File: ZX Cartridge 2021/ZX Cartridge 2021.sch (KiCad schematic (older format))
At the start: 7 parts, among them J1 Cartridge, M1 Mounting, M2 Mounting, M3 Mounting, M4 Mounting, U1 27C512

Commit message: ... and the rest
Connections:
- net ~ROM_0: now also J1.A18 (~ROM_0); no longer J1.A20 (~ROM_2)
- net ~ROM_OE: now also J1.A17 (~ROM_OE); no longer J1.A21 (~ROM_3)
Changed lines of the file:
@@
 	1    0    0    -1
 $EndComp
-Text Label 8225 4400 1    50   ~ 0
+Text Label 8025 4400 1    50   ~ 0
 ~ROM_0
 Text Label 6625 2575 3    50   ~ 0
@@
 Wire Wire Line
 	6725 2550 6725 2900
-Text Label 8325 4400 1    50   ~ 0
+Text Label 7925 4400 1    50   ~ 0
 ~ROM_OE
 Wire Wire Line
@@
 	6925 2450 7025 2550
 Entry Wire Line
-	8325 4525 8225 4425
-Entry Wire Line
-	8425 4525 8325 4425
+	8125 4525 8025 4425
+Entry Wire Line
+	8025 4525 7925 4425
 Entry Wire Line
 	7525 4525 7425 4425
@@
 	8725 3975 8725 3900
 Wire Wire Line
-	8325 3900 8325 4425
-Wire Wire Line
-	8225 3900 8225 4425
+	7925 3900 7925 4425
+Wire Wire Line
+	8025 3900 8025 4425
 Wire Wire Line
 	7525 3900 7525 4425
@@
 NoConn ~ 6825 3900
 NoConn ~ 7625 3900
-NoConn ~ 7925 3900
-NoConn ~ 8025 3900
 NoConn ~ 8125 3900
 NoConn ~ 7025 3900
@@
 	3400 5375 5100 5375
 NoConn ~ 8425 3900
+NoConn ~ 8225 3900
+NoConn ~ 8325 3900
 Wire Bus Line
 	5100 2450 5100 5375

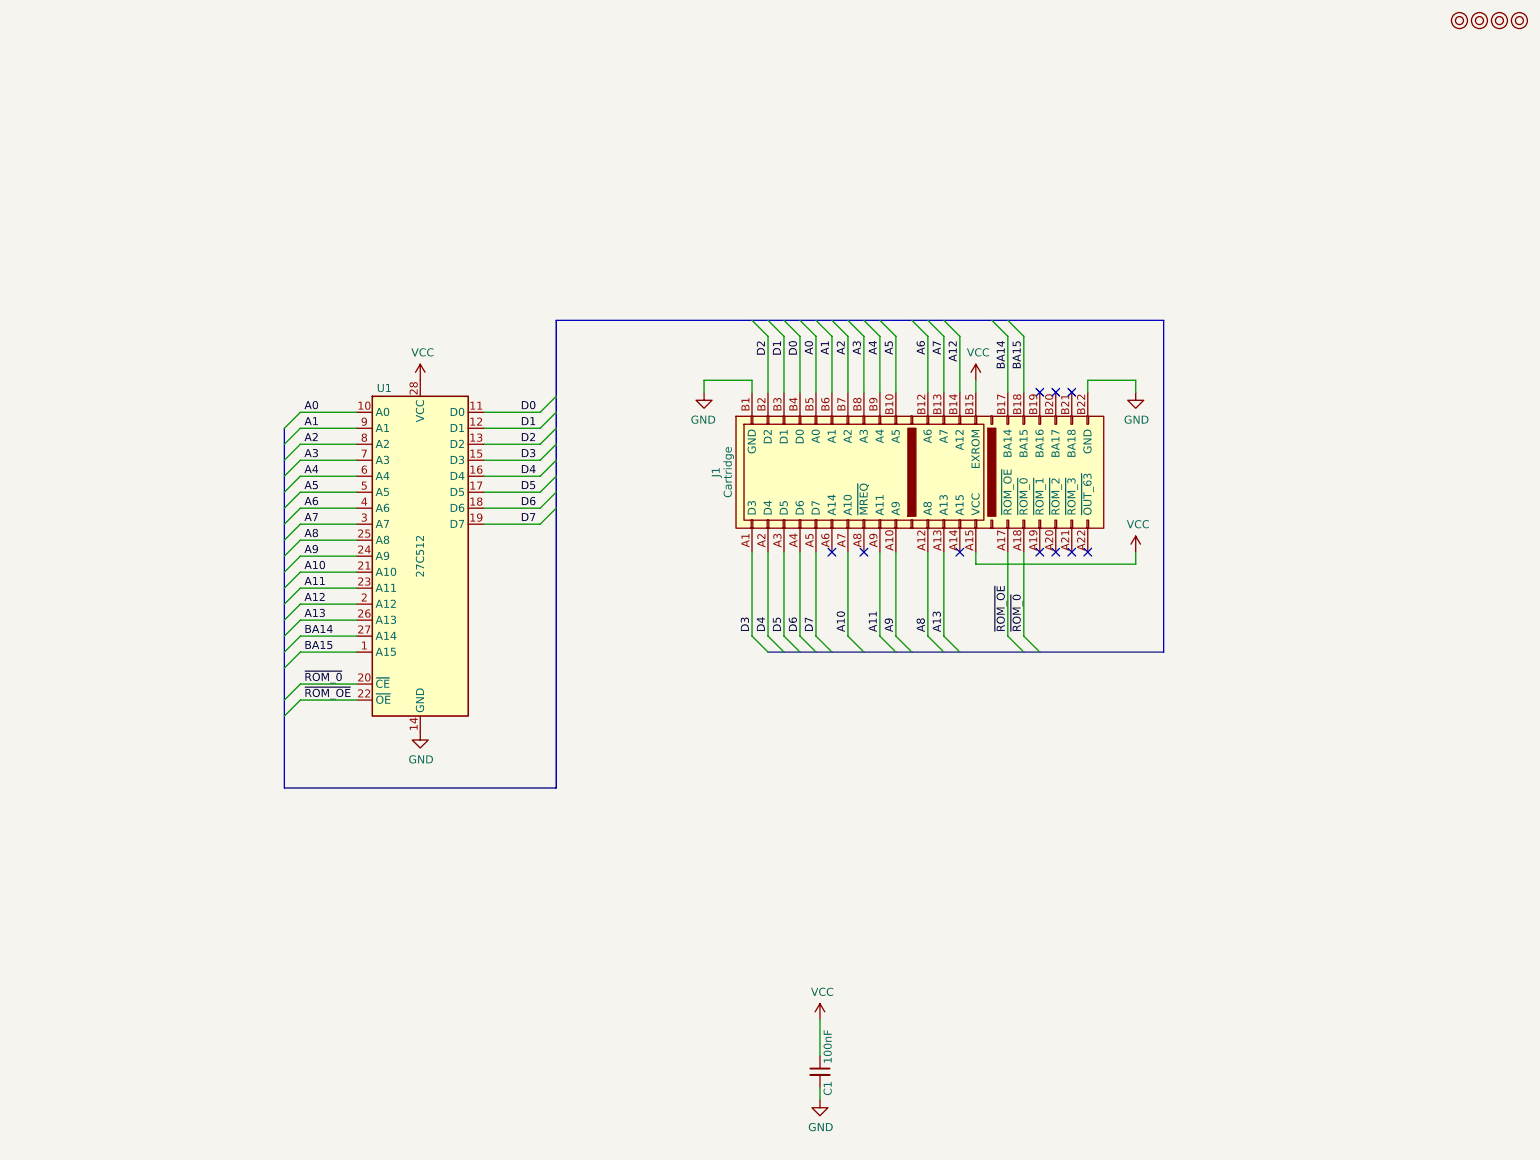
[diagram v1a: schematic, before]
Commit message: Cartridge components thrown in
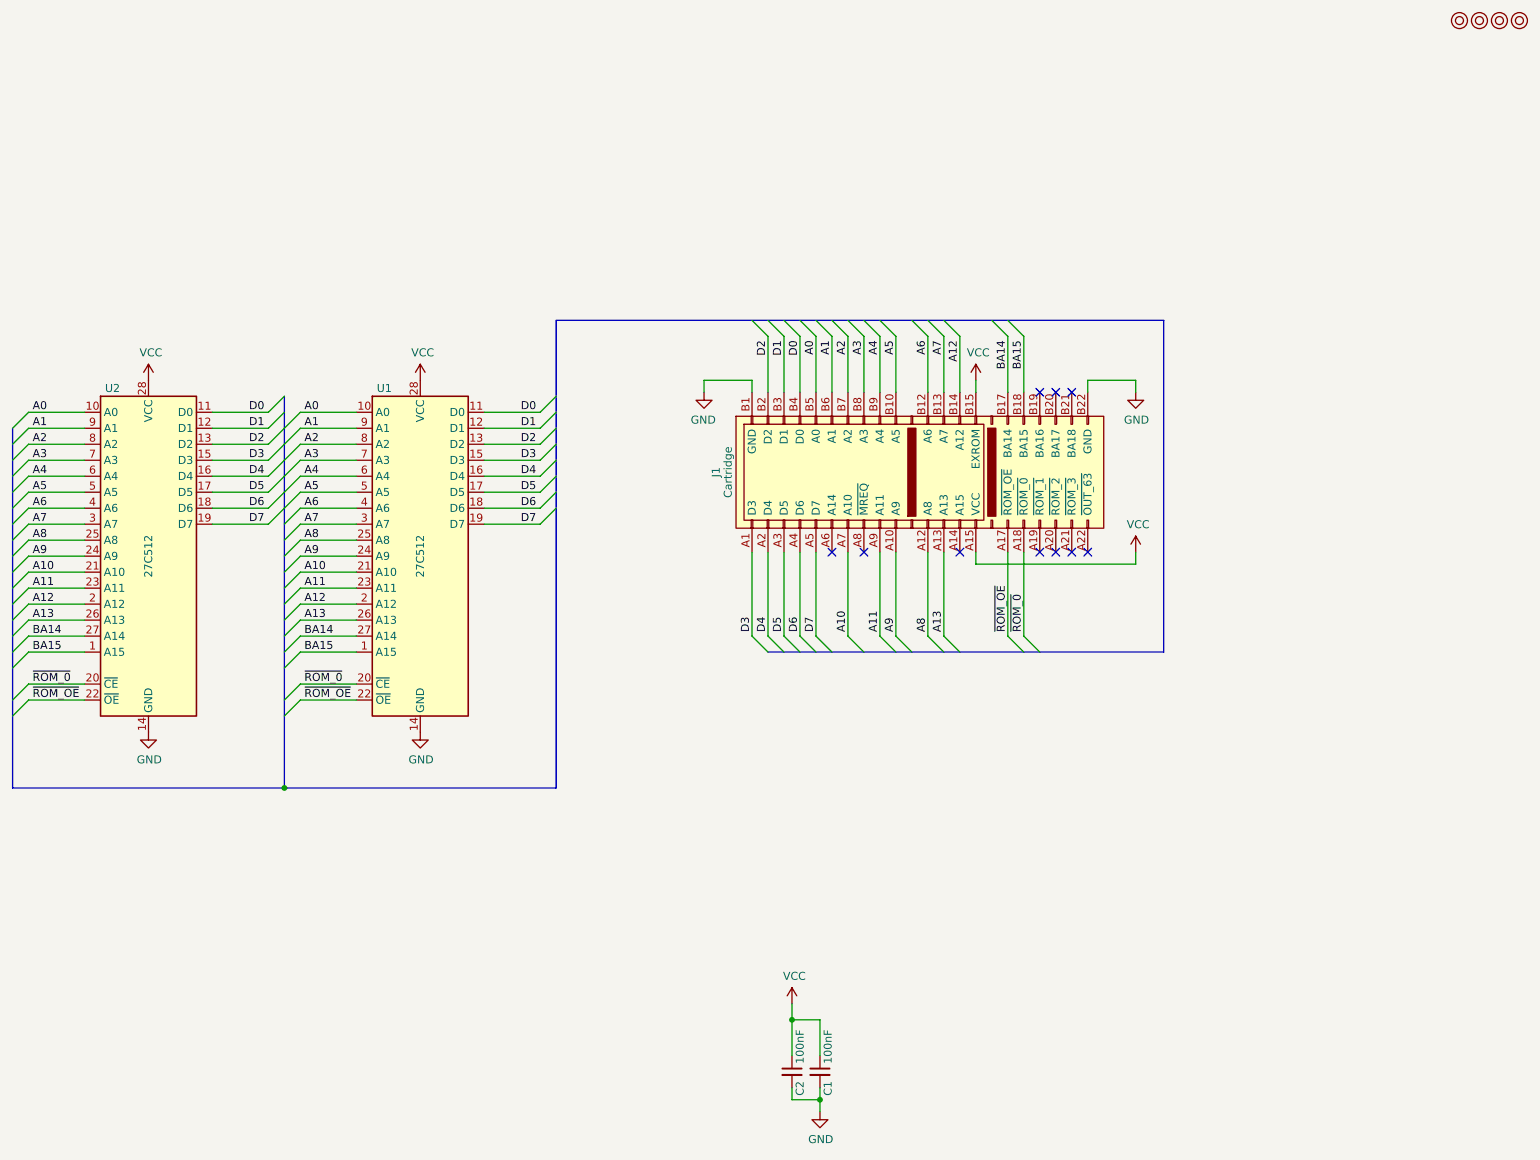
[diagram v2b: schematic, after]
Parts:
- added C2: 100nF, Capacitor_THT:C_Disc_D4.7mm_W2.5mm_P5.00mm, symbol Device:C_Small
- added U2: 27C512, Package_DIP:DIP-28_W15.24mm_Socket_LongPads, symbol Memory_EPROM:27C512
- M1, M2, M3, M4: footprint (none) -> mounting:M3_pin
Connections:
- net A0: now also U2.10 (A0)
- net A1: now also U2.9 (A1)
- net A10: now also U2.21 (A10)
- net A11: now also U2.23 (A11)
- net A12: now also U2.2 (A12)
- net A13: now also U2.26 (A13)
- net A2: now also U2.8 (A2)
- net A3: now also U2.7 (A3)
- net A4: now also U2.6 (A4)
- net A5: now also U2.5 (A5)
- net A6: now also U2.4 (A6)
- net A7: now also U2.3 (A7)
- net A8: now also U2.25 (A8)
- net A9: now also U2.24 (A9)
- net BA14: now also U2.27 (A14)
- net BA15: now also U2.1 (A15)
- net D0: now also U2.11 (D0)
- net D1: now also U2.12 (D1)
- net D2: now also U2.13 (D2)
- net D3: now also U2.15 (D3)
- net D4: now also U2.16 (D4)
- net D5: now also U2.17 (D5)
- net D6: now also U2.18 (D6)
- net D7: now also U2.19 (D7)
- net GND: now also C2.2, U2.14 (GND)
- net VCC: now also C2.1, U2.28 (VCC)
- net ~ROM_0: now also U2.20 (~CE)
- net ~ROM_OE: now also U2.22 (~OE)

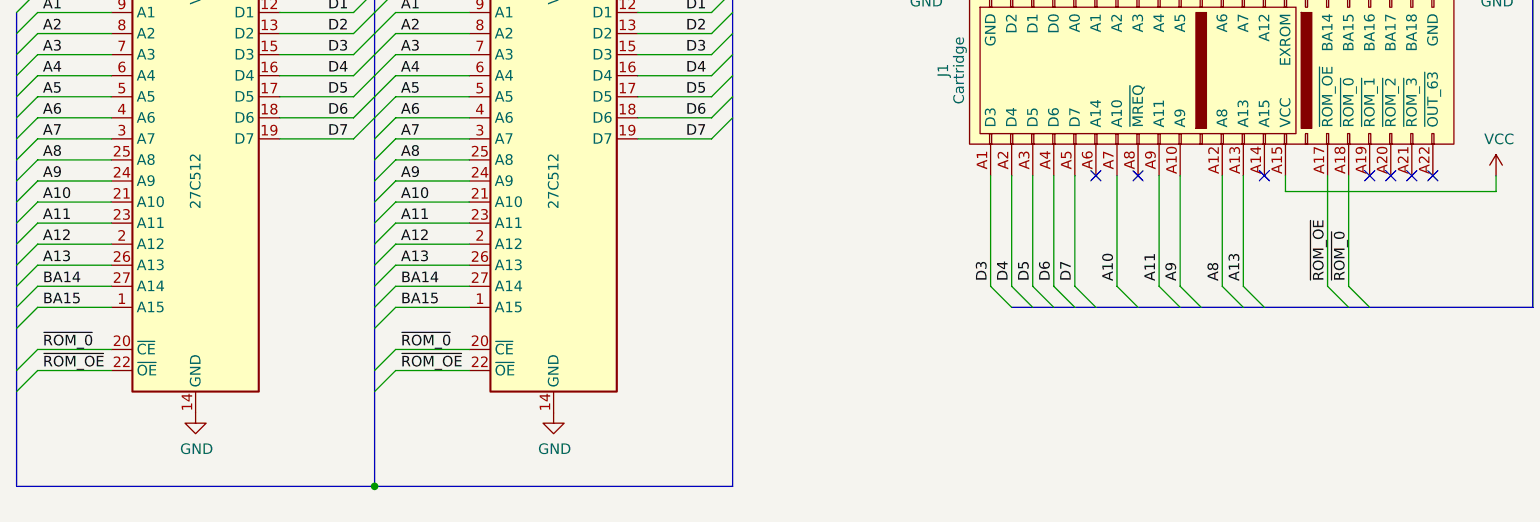
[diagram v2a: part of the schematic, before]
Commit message: 27c512 cartridge layout done
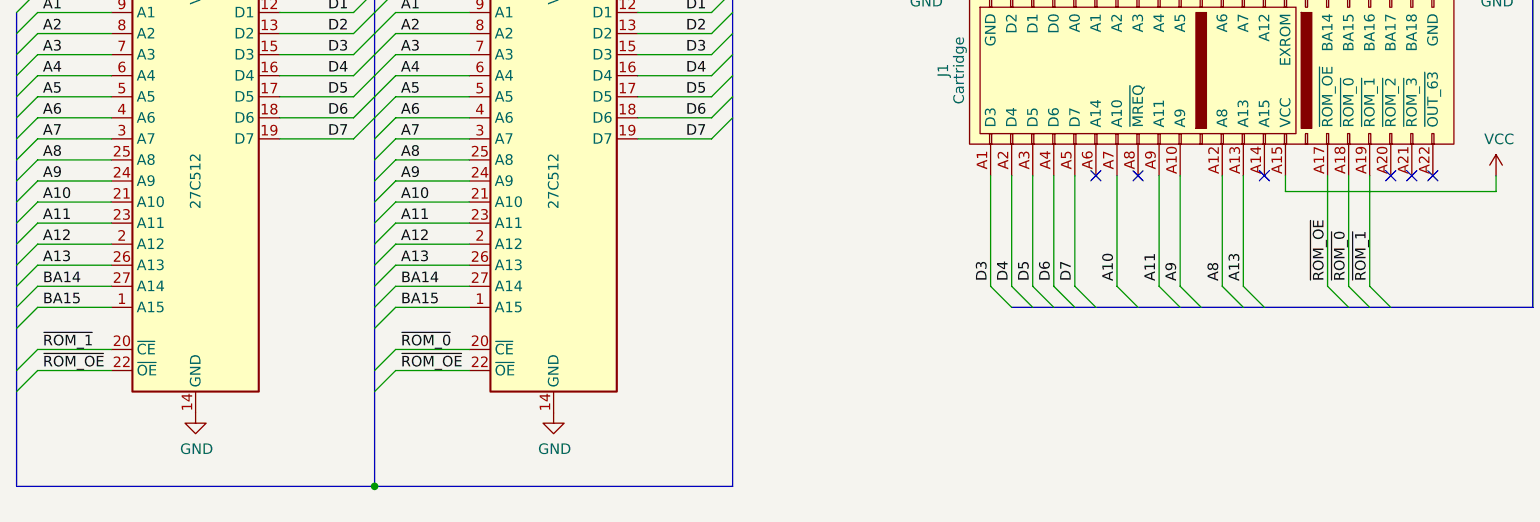
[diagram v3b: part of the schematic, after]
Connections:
- net ~ROM_0: no longer U2.20 (~CE)
- net ~ROM_1: now reaches J1.A19 (~ROM_1)
- net ~ROM_1: now also U2.20 (~CE)
- no-connect marks 10 -> 9
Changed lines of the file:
@@
 NoConn ~ 6825 3900
 NoConn ~ 7625 3900
-NoConn ~ 8125 3900
 NoConn ~ 7025 3900
 NoConn ~ 8125 2900
@@
 	1800 4725 2150 4725
 Text Label 1825 4725 0    50   ~ 0
-~ROM_0
-$Comp
-L power:GND #PWR?
+~ROM_1
+$Comp
+L power:GND #PWR0104
 U 1 1 6072DF1D
 P 2550 5025
-F 0 "#PWR?" H 2550 4775 50  0001 C CNN
+F 0 "#PWR0104" H 2550 4775 50  0001 C CNN
 F 1 "GND" H 2555 4852 50  0000 C CNN
 F 2 "" H 2550 5025 50  0001 C CNN
@@
 $EndComp
 $Comp
-L power:VCC #PWR?
+L power:VCC #PWR0105
 U 1 1 6072DF23
 P 2550 2825
-F 0 "#PWR?" H 2550 2675 50  0001 C CNN
+F 0 "#PWR0105" H 2550 2675 50  0001 C CNN
 F 1 "VCC" H 2565 2998 50  0000 C CNN
 F 2 "" H 2550 2825 50  0001 C CNN
@@
 Wire Wire Line
 	6575 6825 6575 7050
+Text Label 8125 4400 1    50   ~ 0
+~ROM_1
+Entry Wire Line
+	8225 4525 8125 4425
+Wire Wire Line
+	8125 3900 8125 4425
 Wire Bus Line
 	5100 2450 5100 5375

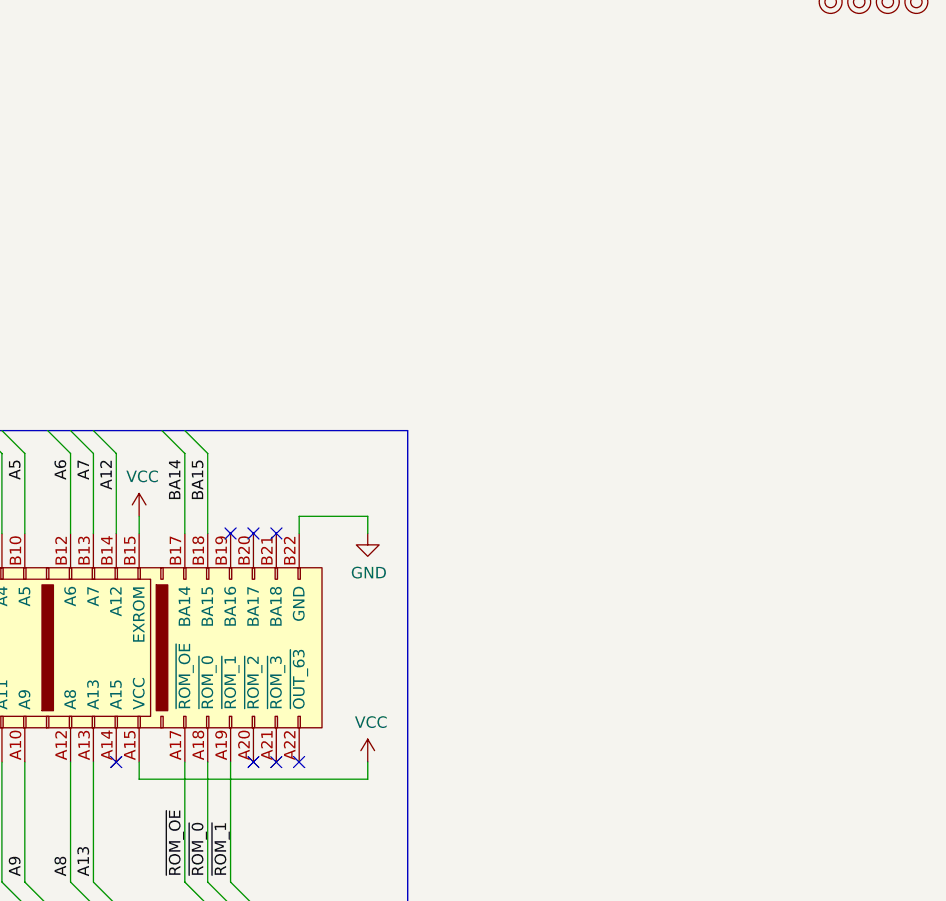
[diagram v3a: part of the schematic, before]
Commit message: Added 27C256 and 27C128 compatibility
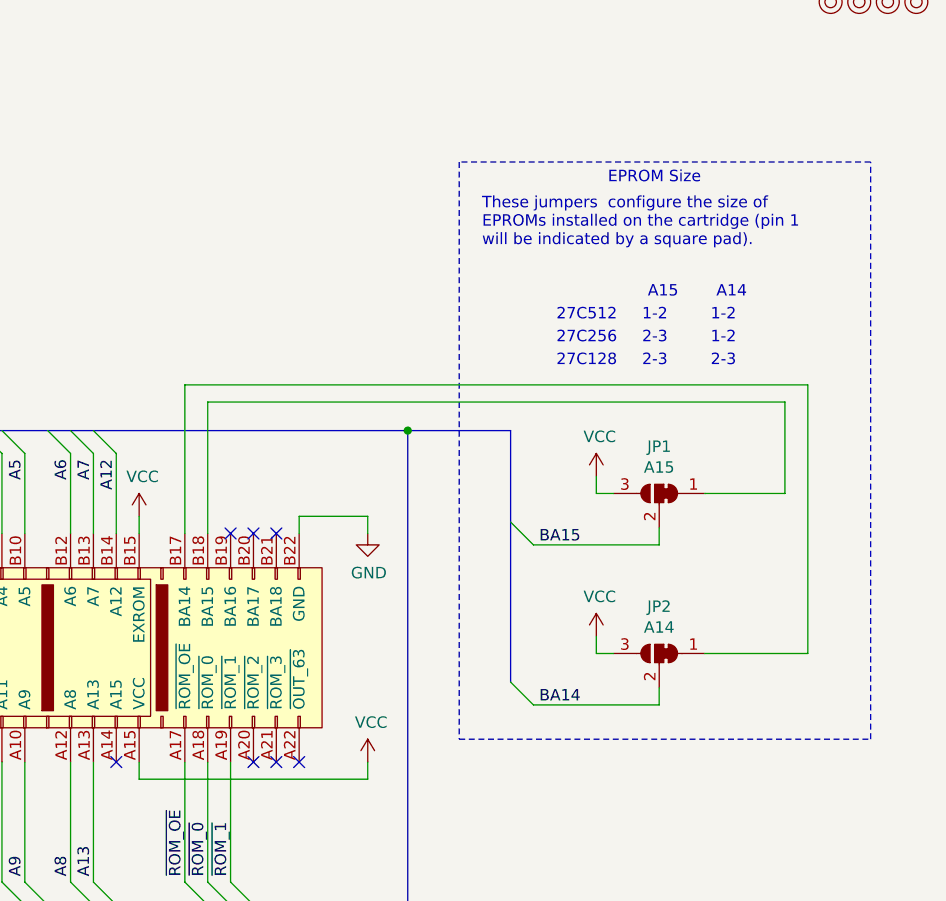
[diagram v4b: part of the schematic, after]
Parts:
- added JP1: A15, solder_bridge:select, symbol solder_select:SolderJumper_3_Bridged12
- added JP2: A14, solder_bridge:select, symbol solder_select:SolderJumper_3_Bridged12
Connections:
- net BA14: now also JP2.2 (C); no longer J1.B17 (BA14)
- net BA15: now also JP1.2 (C); no longer J1.B18 (BA15)
- net VCC: now also JP1.3 (B), JP2.3 (B)
- new net: J1.B17 (BA14), JP2.1 (A)
- new net: J1.B18 (BA15), JP1.1 (A)
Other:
- note added: "1-2"
- note added: "2-3"
- note added: "27C128"
- note added: "27C256"
- note added: "27C512"
- note added: "A14"
- note added: "A15"
- note added: "EPROM Size"
- note added: "These jumpers configure the size of\nEPROMs installed on the cartridge (pin 1\nwill be indicated by a square pad)."
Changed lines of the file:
@@
 Text Label 7525 4400 1    50   ~ 0
 A13
-Text Label 7925 2575 3    50   ~ 0
-BA14
-Text Label 8025 2575 3    50   ~ 0
-BA15
-Wire Wire Line
-	8025 2900 8025 2550
-Wire Wire Line
-	7925 2550 7925 2900
 Wire Wire Line
 	7625 2550 7625 2900
@@
 Text Label 3525 4825 0    50   ~ 0
 ~ROM_OE
-Text Label 3525 4525 0    50   ~ 0
+Text Label 1825 4525 0    50   ~ 0
 BA15
 $Comp
@@
 	1    0    0    -1
 $EndComp
-Text Label 3525 4425 0    50   ~ 0
+Text Label 1825 4425 0    50   ~ 0
 BA14
 Text Label 3525 4325 0    50   ~ 0
@@
 Entry Wire Line
 	7125 2450 7225 2550
-Entry Wire Line
-	7925 2450 8025 2550
-Entry Wire Line
-	7825 2450 7925 2550
-Wire Bus Line
-	8900 2450 8900 4525
 Wire Wire Line
 	7725 2825 7725 2900
@@
 Text Label 1825 4825 0    50   ~ 0
 ~ROM_OE
-Text Label 1825 4525 0    50   ~ 0
-BA15
 $Comp
 L Memory_EPROM:27C512 U2
@@
 	1    0    0    -1
 $EndComp
-Text Label 1825 4425 0    50   ~ 0
-BA14
 Text Label 1825 4325 0    50   ~ 0
 A13
@@
 Wire Wire Line
 	8125 3900 8125 4425
+Text Label 9475 2950 0    50   ~ 0
+BA15
+Text Label 9475 3650 0    50   ~ 0
+BA14
+Entry Wire Line
+	9350 3550 9450 3650
+Entry Wire Line
+	9350 2850 9450 2950
+Wire Wire Line
+	10000 2950 9450 2950
+Wire Wire Line
+	10550 2725 10200 2725
+Wire Wire Line
+	10000 2875 10000 2950
+$Comp
+L power:VCC #PWR03
+U 1 1 60482C7C
+P 9725 2650
+F 0 "#PWR03" H 9725 2500 50  0001 C CNN
+F 1 "VCC" H 9740 2823 50  0000 C CNN
+F 2 "" H 9725 2650 50  0001 C CNN
+F 3 "" H 9725 2650 50  0001 C CNN
+	1    9725 2650
+	1    0    0    -1
+$EndComp
+Wire Wire Line
+	9725 2725 9725 2650
+Wire Wire Line
+	9800 2725 9725 2725
+$Comp
+L solder_select:SolderJumper_3_Bridged12 JP1
+U 1 1 60482C74
+P 10000 2725
+F 0 "JP1" H 10000 2930 50  0000 C CNN
+F 1 "A15" H 10000 2839 50  0000 C CNN
+F 2 "solder_bridge:select" H 10000 2725 50  0001 C CNN
+F 3 "~" H 10000 2725 50  0001 C CNN
+	1    10000 2725
+	-1   0    0    -1
+$EndComp
+Wire Wire Line
+	10000 3650 9450 3650
+Wire Wire Line
+	10000 3575 10000 3650
+$Comp
+L power:VCC #PWR04
+U 1 1 6045383E
+P 9725 3350
+F 0 "#PWR04" H 9725 3200 50  0001 C CNN
+F 1 "VCC" H 9740 3523 50  0000 C CNN
+F 2 "" H 9725 3350 50  0001 C CNN
+F 3 "" H 9725 3350 50  0001 C CNN
+	1    9725 3350
+	1    0    0    -1
+$EndComp
+Wire Wire Line
+	9725 3425 9725 3350
+Wire Wire Line
+	9800 3425 9725 3425
+$Comp
+L solder_select:SolderJumper_3_Bridged12 JP2
+U 1 1 60439B63
+P 10000 3425
+F 0 "JP2" H 10000 3630 50  0000 C CNN
+F 1 "A14" H 10000 3539 50  0000 C CNN
+F 2 "solder_bridge:select" H 10000 3425 50  0001 C CNN
+F 3 "~" H 10000 3425 50  0001 C CNN
+	1    10000 3425
+	-1   0    0    -1
+$EndComp
+Wire Wire Line
+	10550 2725 10550 2325
+Wire Wire Line
+	8025 2325 8025 2900
+Wire Wire Line
+	7925 2250 7925 2900
+Wire Wire Line
+	10200 3425 10650 3425
+Wire Wire Line
+	10650 2250 10650 3425
+Wire Bus Line
+	8900 2450 8900 4525
+Wire Wire Line
+	7925 2250 10650 2250
+Wire Wire Line
+	8025 2325 10550 2325
+Wire Bus Line
+	9350 2450 8900 2450
+Connection ~ 8900 2450
+Wire Notes Line
+	9125 3800 10925 3800
+Wire Notes Line
+	10925 3800 10925 1275
+Wire Notes Line
+	10925 1275 9125 1275
+Wire Notes Line
+	9125 1275 9125 3800
+Text Notes 9775 1375 0    50   ~ 0
+EPROM Size
+Text Notes 9225 1650 0    50   ~ 0
+These jumpers  configure the size of\nEPROMs installed on the cartridge (pin 1\nwill be indicated by a square pad).
+Text Notes 9950 1875 0    50   ~ 0
+A15
+Text Notes 10250 1875 0    50   ~ 0
+A14
+Text Notes 9550 1975 0    50   ~ 0
+27C512
+Text Notes 9550 2075 0    50   ~ 0
+27C256
+Text Notes 9550 2175 0    50   ~ 0
+27C128
+Text Notes 9925 1975 0    50   ~ 0
+1-2
+Text Notes 10225 2075 0    50   ~ 0
+1-2
+Text Notes 9925 2075 0    50   ~ 0
+2-3
+Text Notes 9925 2175 0    50   ~ 0
+2-3
+Text Notes 10225 2175 0    50   ~ 0
+2-3
+Text Notes 10225 1975 0    50   ~ 0
+1-2
+Text Label 3525 4525 0    50   ~ 0
+BA15
+Text Label 3525 4425 0    50   ~ 0
+BA14
+Wire Bus Line
+	9350 2450 9350 3550
 Wire Bus Line
 	5100 2450 5100 5375
